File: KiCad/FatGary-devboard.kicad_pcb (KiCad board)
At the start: 4 copper layers, 91.2 x 52 mm, 10 parts, among them J1 USB_B_Micro, J2 Conn_02x01, J3 Conn_01x01, U1 PLCC-84-Plug, U2 Fat_Gary_SMD_socket, U3 Fat_Gary_TH_socket

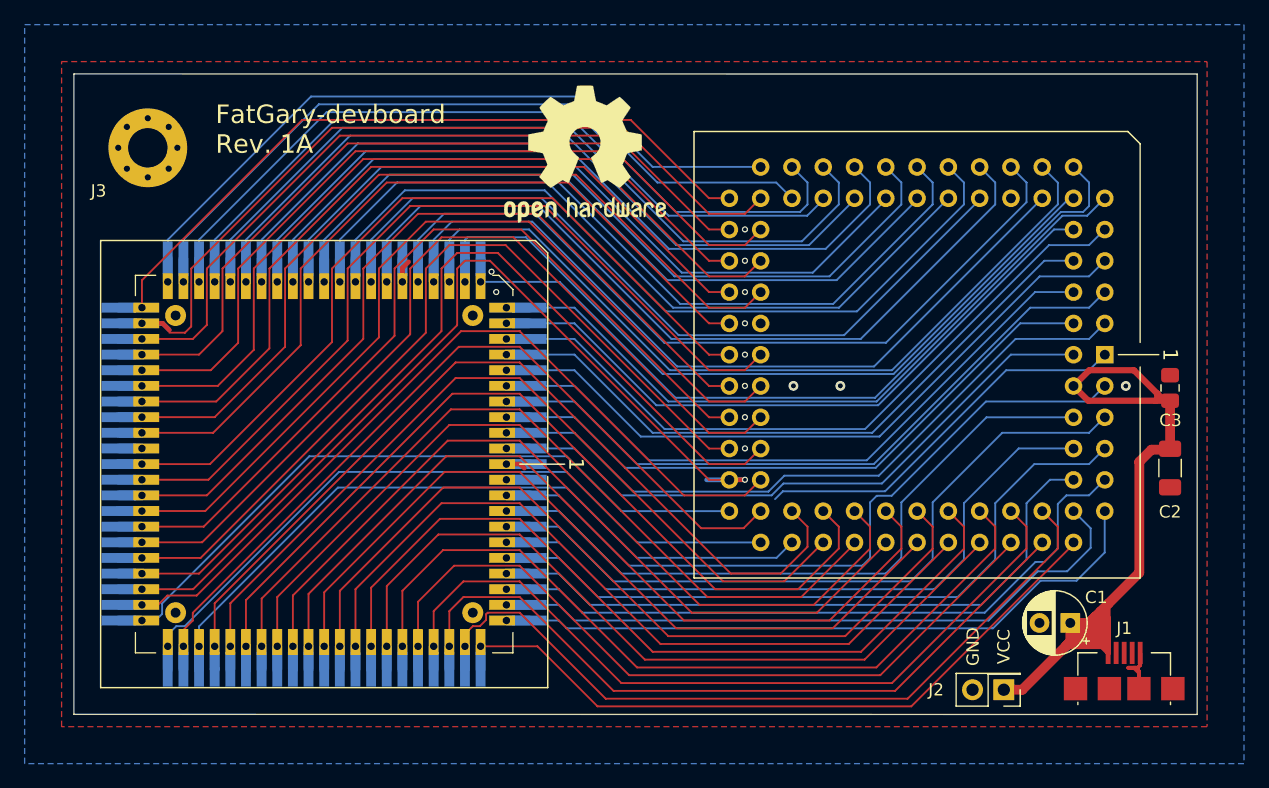
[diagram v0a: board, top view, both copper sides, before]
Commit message: Change to footprint with longer pads for the PLCC-84 smd plug
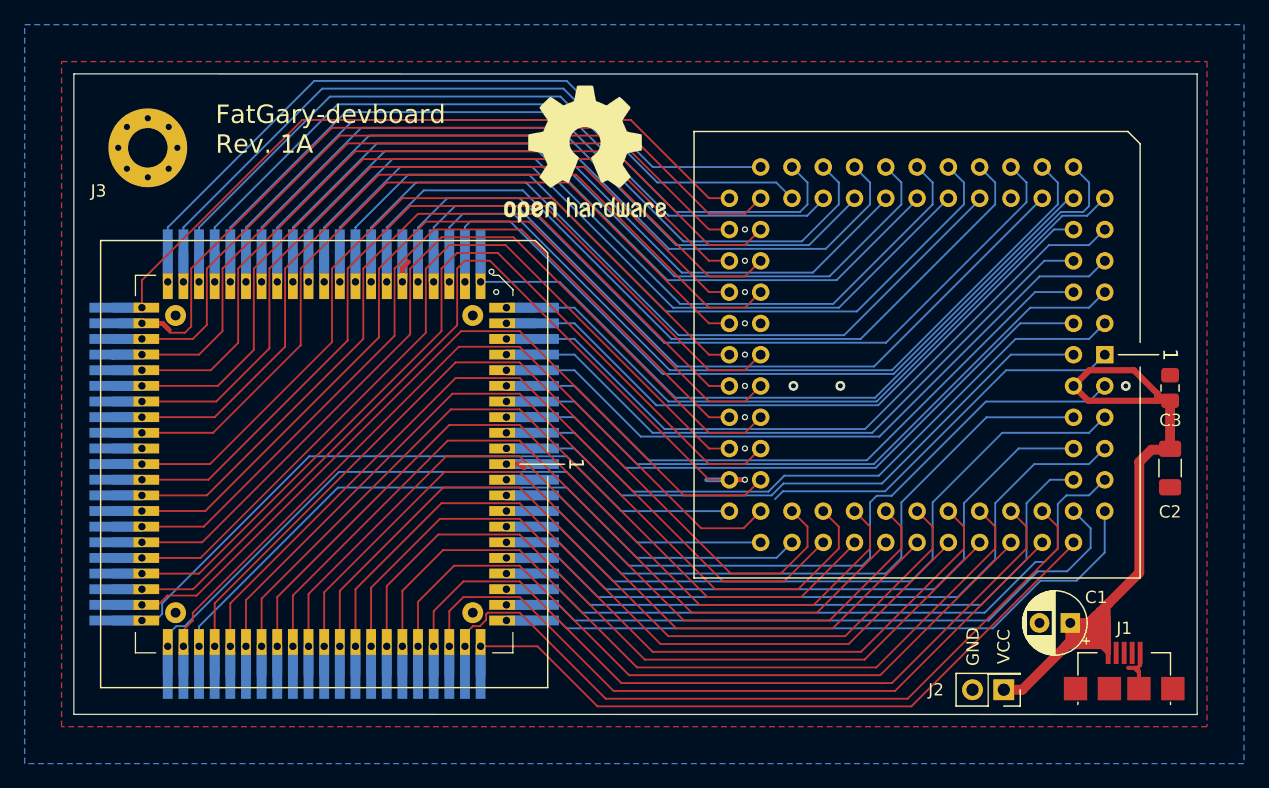
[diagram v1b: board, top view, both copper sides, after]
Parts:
- U1: footprint FatGary-devboard:PLCC-84_Plug_P1.27mm_mirrored -> FatGary-devboard:PLCC-84_Plug_P1.27mm_mirrored_extended_pads
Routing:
- net A21: track 63.5 -> 65.2 mm
- net A14: track 58.7 -> 60.4 mm
- net A13: track 60.5 -> 62.2 mm
- net FC1: track 61.9 -> 63.5 mm
- net DSACK0: track 60.7 -> 62.4 mm
- net SIZ1: track 65.2 -> 66.8 mm
- net RW: track 64.7 -> 66.3 mm
- net FC2: track 66.3 -> 67.9 mm
- net AS: track 62.5 -> 64.1 mm
- net A20: track 67.0 -> 68.7 mm
- net A19: track 64.0 -> 65.6 mm
- net A18: track 66.1 -> 67.8 mm
- net SIZ0: track 61.7 -> 63.3 mm
- net FC0: track 65.5 -> 67.1 mm
- net A1: track 65.7 -> 67.4 mm
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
